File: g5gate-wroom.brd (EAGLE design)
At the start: 33.2 x 69.1 mm, 28 parts, among them IC1 TCAN1051HGV, U2 XN04312, U8 NCP1117LPST50T3G

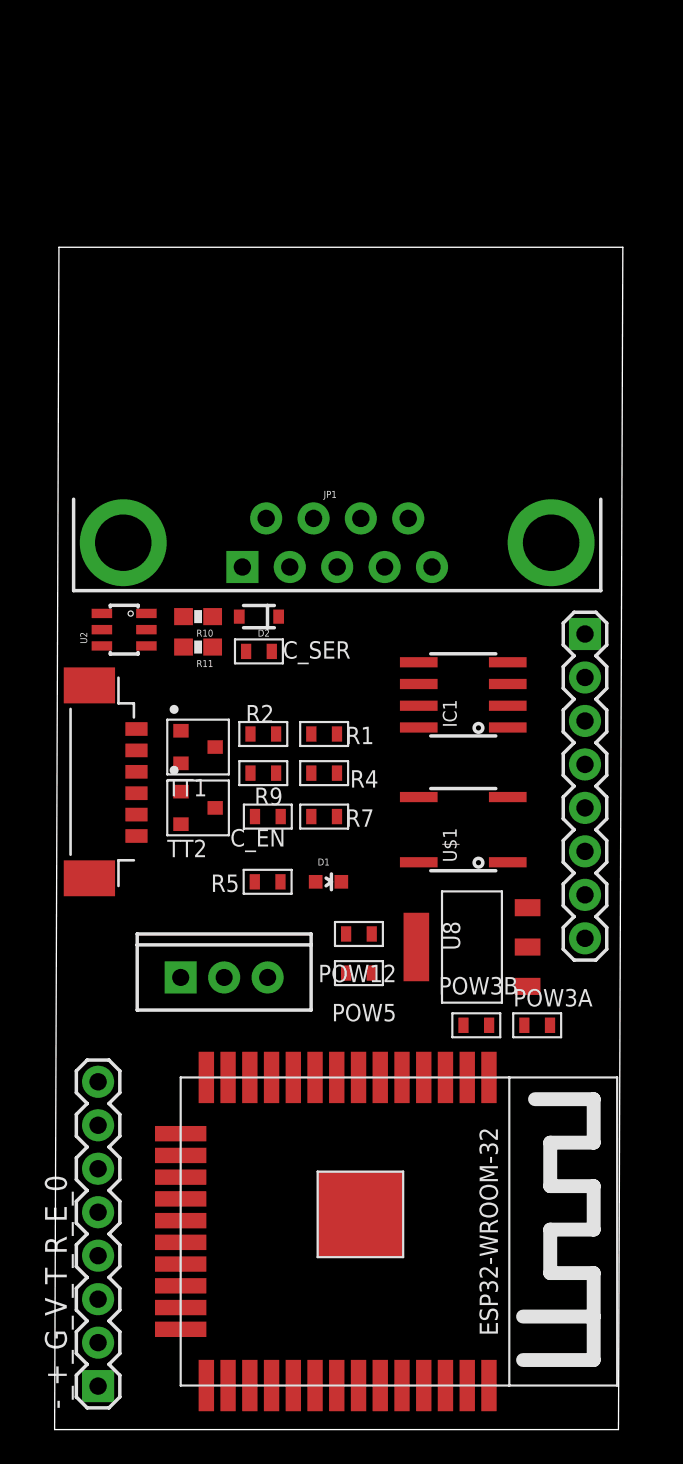
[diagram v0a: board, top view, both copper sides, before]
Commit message: Add touchscreen header directly to board
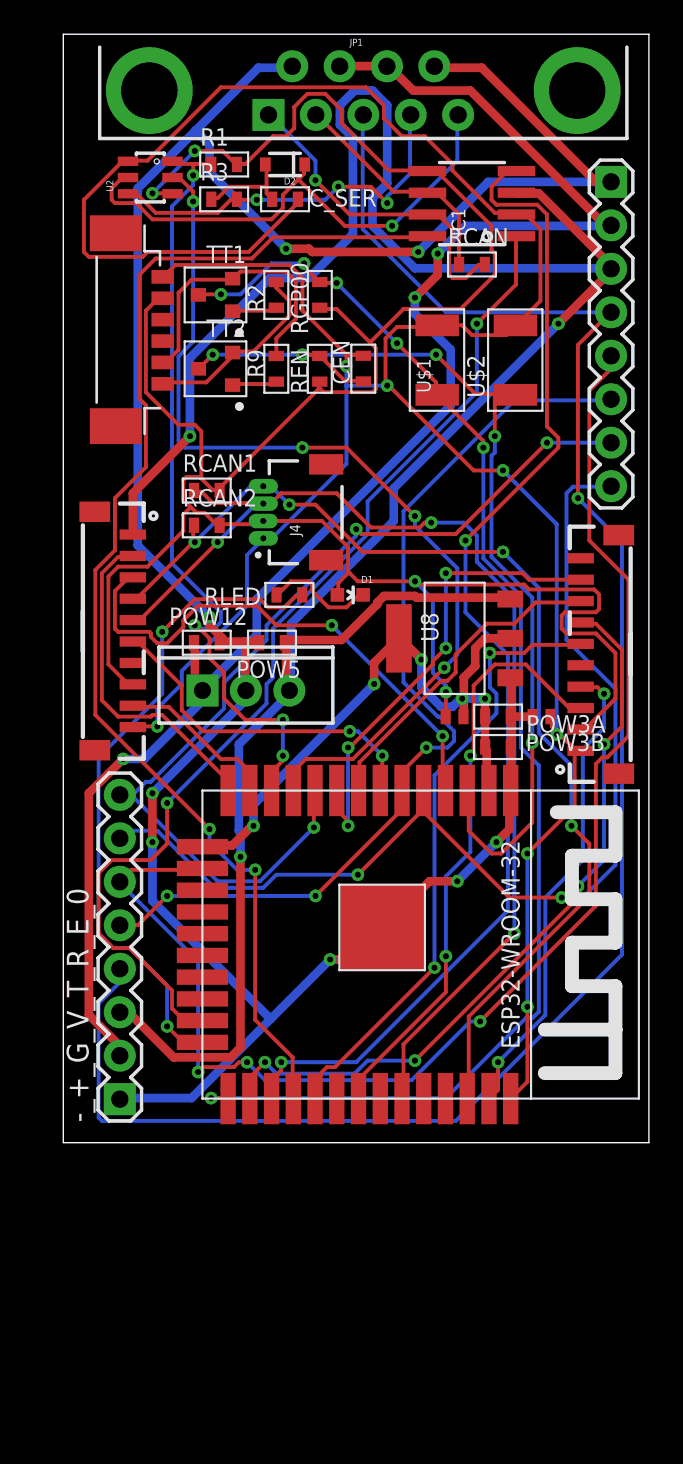
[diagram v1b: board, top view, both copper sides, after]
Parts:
- removed C_EN: (no value), MF_Passives:C0603
- removed R10, R11: 10K, SparkFun-Resistors:0603-RES
- removed R7: (no value), 00jim:R0603
- added CEN: (no value), MF_Passives:C0603
- added J2, J3: (no value), SparkFun-Connectors:1X10-1.25MM
- added J4: Vertical Qwiic Connector, 00jim:JST04_1MM_HOLES
- added R3, RCAN, RCAN1, RCAN2, REN, RGP00, RLED: (no value), 00jim:R0603
- added U$2: AMAZON_BUTTONB2010, 00jim:C2010
- R4, R5: device 00jim:R0603 -> 00jim:R0603_JMP
- U$1: value AMAZON_BUTTON -> AMAZON_BUTTONB2010; device 00jim:AMAZON_BUTTON -> 00jim:C2010
- moved R1 33.8 mm to (9.91, 57.4), turned to 0 degrees
- moved IC1 28.7 mm to (24.4, 55.1)
- moved U$1 27.5 mm to (22.4, 46.0)
- moved D2 26.5 mm to (13.5, 57.4)
- moved J1 26.5 mm to (4.83, 47.8)
- moved JP1 26.5 mm to (18.0, 61.7)
- moved U2 26.5 mm to (5.59, 56.6)
- moved C_SER 26.5 mm to (13.5, 55.4)
- moved -_+_G_V_T_R_E_1 26.5 mm to (32.5, 56.4)
- moved TT1 26.4 mm to (9.40, 49.8), turned to 180 degrees
- moved TT2 25.7 mm to (9.40, 45.5), turned to 180 degrees
- moved R2 25.7 mm to (13.0, 49.8), turned to 270 degrees
- moved R9 23.6 mm to (13.0, 45.5), turned to 270 degrees
- moved POW5 20.0 mm to (12.7, 29.5)
- moved POW12 19.2 mm to (8.89, 29.5), turned to 0 degrees
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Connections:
- removed net IO14: R5.P$1, U$3.IO14
- removed net SCL: U$3.IO22
- removed net SDA: U$3.IO21
- new net BUZZ: J2.9, U$3.IO14
- new net CLK: J3.5
- new net GND_HC: -_+_G_V_T_R_E_0.1, -_+_G_V_T_R_E_1.1, JP1.6, JP1.9, POW12.P$2, POW3A.P$2, POW3B.P$2, POW5.P$2, R4.P$1, U$3.GND1, U$3.GND4, U3.GND, U8.P$2
- new net GPS_RX: J2.3, U$3.SENSOR_VP
- new net GPS_TX: J2.2, U$3.IO12
- new net LED: J2.7
- new net MISO: J3.3, U$3.IO19
- new net MOSI: J3.4, U$3.IO23
- new net RX3: -_+_G_V_T_R_E_0.5, -_+_G_V_T_R_E_1.6, U$3.IO34
- new net SCL1: J2.4, J4.P$4, RCAN2.P$1, U$3.IO22
- new net SCLK: U$3.IO18
- new net SDA1: J2.5, J4.P$3, RCAN1.P$1, U$3.IO21
- new net SWITCH: J2.6, U$3.IO35
- new net TCH_CS: J3.7, U$3.IO4
- new net TFT_CS: J3.6, U$3.IO5
- new net TFT_DC: J3.8, U$3.IO32
- new net TFT_RST: J3.9, U$3.IO33
- new net TX3: -_+_G_V_T_R_E_0.6, -_+_G_V_T_R_E_1.5, U$3.IO13
- new net VCC_HC: POW3A.P$1, POW3B.P$1, R5.P$1, U$3.3V3, U$3.GND2, U8.P$1, U8.P$3
- net CANRX: now also U$3.IO16; no longer U$3.IO18
- net CANTX: now also U$3.IO15; no longer U$3.IO19
- net CAN_H: now also RCAN.P$2
- net CAN_L: now also RCAN.P$1
- net DB9_TX: now also R1.P$1; no longer R11.1
- net EN: now also CEN.P$1, REN.P$1, U$2.P$1; no longer C_EN.P$1, R4.P$1
- net GND: now also CEN.P$2, J2.10, J3.1, J4.P$1, R4.P$2, U$1.P$2, U$2.P$2; no longer -_+_G_V_T_R_E_0.1, -_+_G_V_T_R_E_0.3, -_+_G_V_T_R_E_0.7, -_+_G_V_T_R_E_1.1, -_+_G_V_T_R_E_1.3, -_+_G_V_T_R_E_1.7, C_EN.P$2, JP1.6, JP1.9, POW12.P$2, POW3A.P$2, POW3B.P$2, POW5.P$2, R7.P$2, U$1.2, U$1.3, U$3.GND1, U$3.GND2, U$3.GND4, U3.GND, U8.P$2
- net IO00: now also RGP00.P$1, U$1.P$1; no longer R1.P$1, U$1.1, U$1.4
- net IO02: now also RLED.P$1; no longer R7.P$1
- net N$2: now also RLED.P$2; no longer R5.P$2
- net N$4: now also R3.P$1; no longer R10.1
- net RAW: no longer U8.P$4
- net RS-OUT: now also R3.P$2; no longer R10.2
- net RX2: now also -_+_G_V_T_R_E_0.7, -_+_G_V_T_R_E_1.8, U$3.SENSOR_VN; no longer -_+_G_V_T_R_E_0.5, -_+_G_V_T_R_E_1.6, U$3.IO33
- net TX2: now also -_+_G_V_T_R_E_0.8, -_+_G_V_T_R_E_1.7; no longer -_+_G_V_T_R_E_0.6, -_+_G_V_T_R_E_1.5
- net UNITID: now also -_+_G_V_T_R_E_0.4, -_+_G_V_T_R_E_1.4; no longer -_+_G_V_T_R_E_0.8, -_+_G_V_T_R_E_1.8
- net VCC: now also J2.8, J3.2, J4.P$2, R5.P$2, RCAN1.P$2, RCAN2.P$2, REN.P$2, RGP00.P$2; no longer -_+_G_V_T_R_E_0.4, -_+_G_V_T_R_E_1.4, POW3A.P$1, POW3B.P$1, R11.2, R4.P$2, U$3.3V3, U8.P$1, U8.P$3
- net VCC_50: now also -_+_G_V_T_R_E_0.3, -_+_G_V_T_R_E_1.3, J2.1, U8.P$4
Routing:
- net GND: track 0.00 -> 164.8 mm, vias 0 -> 7
- net GND_HC: track 0.00 -> 152.7 mm, vias 0 -> 8
- net VCC_50: track 0.00 -> 145.7 mm, vias 0 -> 3
- net VCC: track 0.00 -> 141.1 mm, vias 0 -> 4
- net UNITID: track 0.00 -> 106.5 mm, vias 0 -> 1
- net RAW: track 0.00 -> 92.1 mm, vias 0 -> 3
- net TX3: track 0.00 -> 80.9 mm, vias 0 -> 3
- net IO00: track 0.00 -> 79.1 mm, vias 0 -> 6
- net CAN_S: track 0.00 -> 72.7 mm, vias 0 -> 2
- net CANRX: track 0.00 -> 69.7 mm, vias 0 -> 2
- net SDA1: track 0.00 -> 65.4 mm, vias 0 -> 3
- net SCL1: track 0.00 -> 64.0 mm, vias 0 -> 4
- net RX2: track 0.00 -> 63.3 mm, vias 0 -> 2
- net CANTX: track 0.00 -> 61.0 mm, vias 0 -> 2
- net EN: track 0.00 -> 58.7 mm, vias 0 -> 5
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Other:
- board size 33.2 x 69.1 mm -> 34.2 x 64.8 mm

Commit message: wroom test two sided
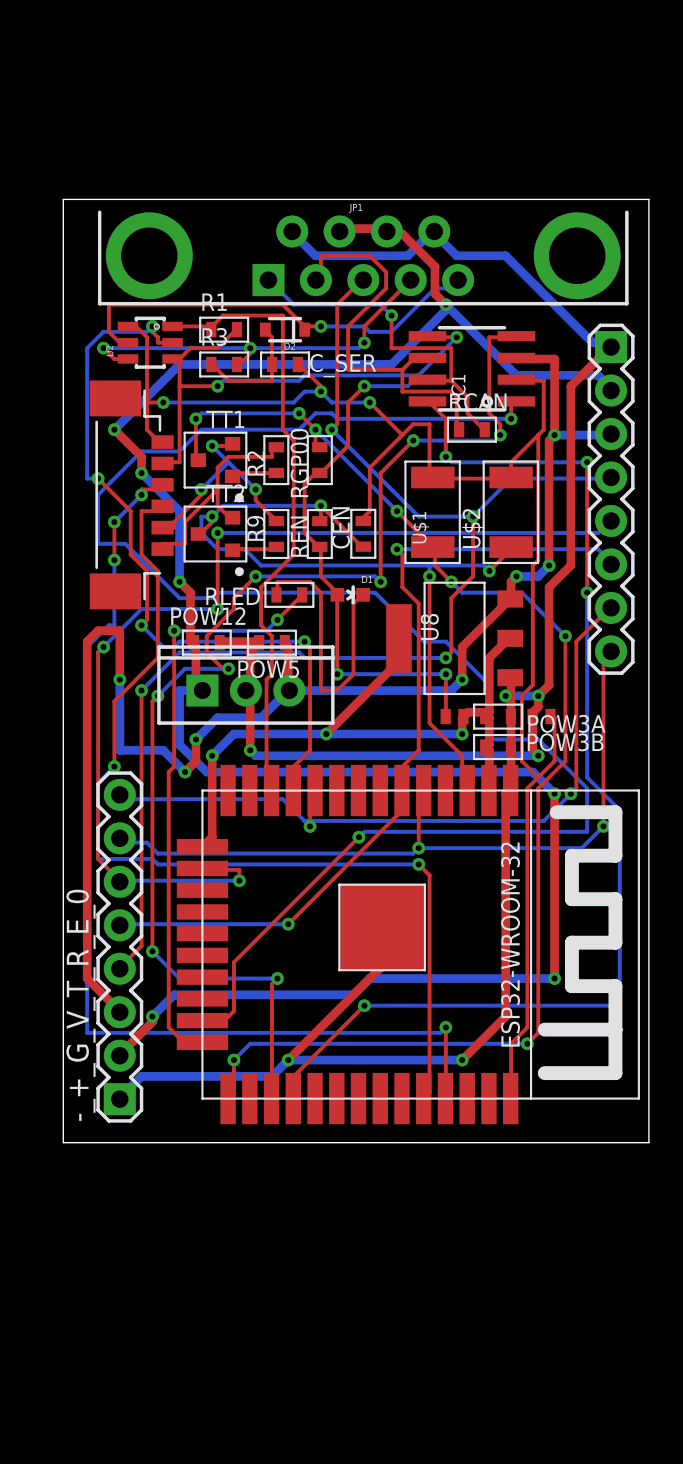
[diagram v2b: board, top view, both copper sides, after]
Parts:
- removed J2, J3: (no value), SparkFun-Connectors:1X10-1.25MM
- removed J4: Vertical Qwiic Connector, 00jim:JST04_1MM_HOLES
- removed RCAN1, RCAN2: (no value), 00jim:R0603
- moved -_+_G_V_T_R_E_1 9.65 mm to (32.5, 46.7)
- moved CEN 9.65 mm to (18.0, 35.8)
- moved C_SER 9.65 mm to (13.5, 45.7)
- moved D2 9.65 mm to (13.5, 47.8)
- moved IC1 9.65 mm to (24.4, 45.5)
- moved J1 9.65 mm to (4.83, 38.1)
- moved JP1 9.65 mm to (18.0, 52.1)
- moved R1 9.65 mm to (9.91, 47.8)
- moved R2 9.65 mm to (13.0, 40.1)
- moved R3 9.65 mm to (9.91, 45.7)
- moved R9 9.65 mm to (13.0, 35.8)
- moved RCAN 9.65 mm to (24.4, 41.9)
- moved REN 9.65 mm to (15.5, 35.8)
- moved RGP00 9.65 mm to (15.5, 40.1)
- moved TT1 9.65 mm to (9.40, 40.1)
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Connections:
- removed net CLK: J3.5
- removed net IO02: RLED.P$1, U$3.IO2
- removed net RX0: J1.4
- removed net TX0: J1.3
- net BUZZ: no longer J2.9
- net GND: no longer J2.10, J3.1, J4.P$1
- net GPS_RX: no longer J2.3
- net GPS_TX: no longer J2.2
- net LED: now also RLED.P$1, U$3.IO2; no longer J2.7
- net MISO: no longer J3.3
- net MOSI: no longer J3.4
- net RXI: now also J1.4
- net SCL1: no longer J2.4, J4.P$4, RCAN2.P$1
- net SDA1: no longer J2.5, J4.P$3, RCAN1.P$1
- net SWITCH: no longer J2.6
- net TCH_CS: no longer J3.7
- net TFT_CS: no longer J3.6
- net TFT_DC: no longer J3.8
- net TFT_RST: no longer J3.9
- net TXO: now also J1.3
- net VCC: no longer J2.8, J3.2, J4.P$2, RCAN1.P$2, RCAN2.P$2
- net VCC_50: no longer J2.1
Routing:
- net VCC: track 141.1 -> 62.6 mm, vias 4 -> 5
- net GND: track 164.8 -> 94.5 mm, vias 7 -> 3
- net SDA1: track 65.4 -> 0.00 mm, vias 3 -> 0
- net SCL1: track 64.0 -> 0.00 mm, vias 4 -> 0
- net VCC_50: track 145.7 -> 85.3 mm, vias 3 -> 7
- net TXO: track 0.00 -> 59.8 mm, vias 0 -> 4
- net RXI: track 0.00 -> 56.5 mm, vias 0 -> 2
- net TCH_CS: track 43.9 -> 0.00 mm, vias 4 -> 0
- net IO02: track 38.7 -> 0.00 mm, vias 2 -> 0
- net CANTX: track 61.0 -> 98.2 mm
- net TFT_CS: track 36.4 -> 0.00 mm, vias 2 -> 0
- net MISO: track 34.7 -> 0.00 mm, vias 2 -> 0
- net RAW: track 92.1 -> 126.8 mm, vias 3 -> 7
- net LED: track 0.00 -> 34.1 mm, vias 0 -> 2
- net UNITID: track 106.5 -> 73.4 mm, vias 1 -> 4
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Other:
- board size 34.2 x 64.8 mm -> 34.2 x 55.1 mm
